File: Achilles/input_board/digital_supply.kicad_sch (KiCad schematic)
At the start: 16 parts, among them U17 TPS565201, U18 INA180A3

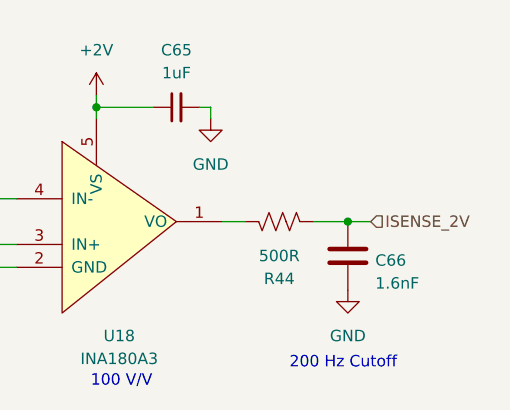
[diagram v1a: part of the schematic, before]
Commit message: Resize boost caps in sim; update pcb with PNs
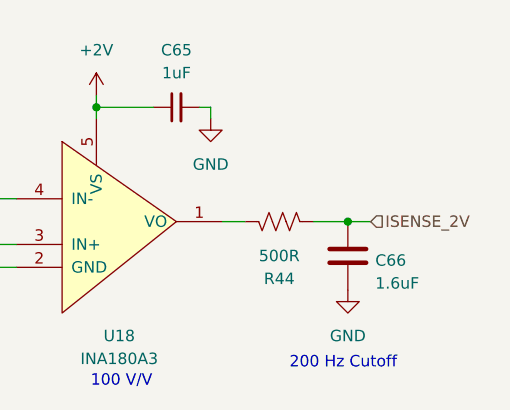
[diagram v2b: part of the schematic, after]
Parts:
- C66: value 1.6nF -> 1.6uF
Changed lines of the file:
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@@
 			)
 		)
-		(property "Value" "1.6nF"
+		(property "Value" "1.6uF"
 			(at 260.858 133.858 0)
 			(effects
